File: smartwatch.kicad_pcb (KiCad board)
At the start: 2 copper layers, 40 x 40 mm, 46 parts, among them IC1 LTC4413EDD-1#PBF, IC2 MIA-M10Q-00B, J1 Conn_01x01_Pin, J2 Conn_01x01_Pin, J3 5022441530, J5 Conn_01x04_Socket, U1 NRF52832-QFAA-R, U10 AP2127K-1.8, U2 AP2112K-3.3TRG1, U3 MAX30102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

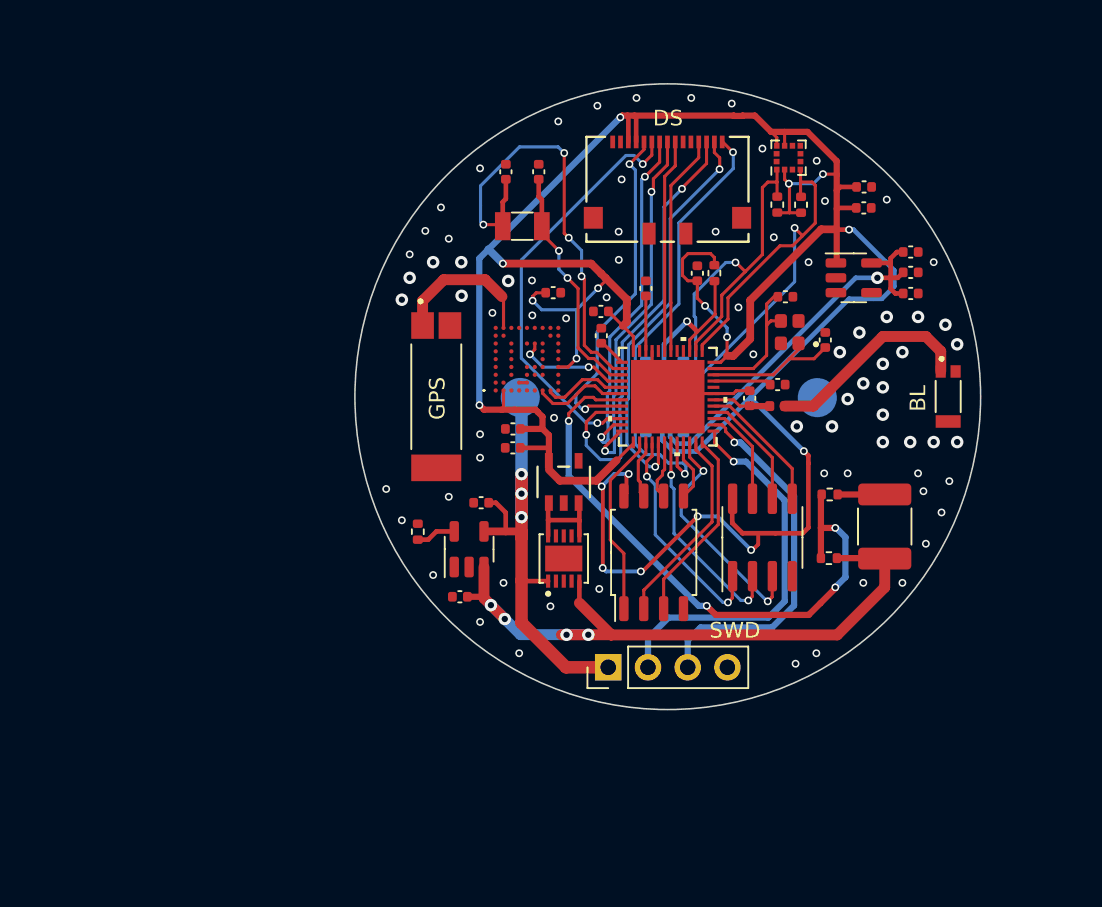
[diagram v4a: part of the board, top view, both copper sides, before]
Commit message: changed gps module
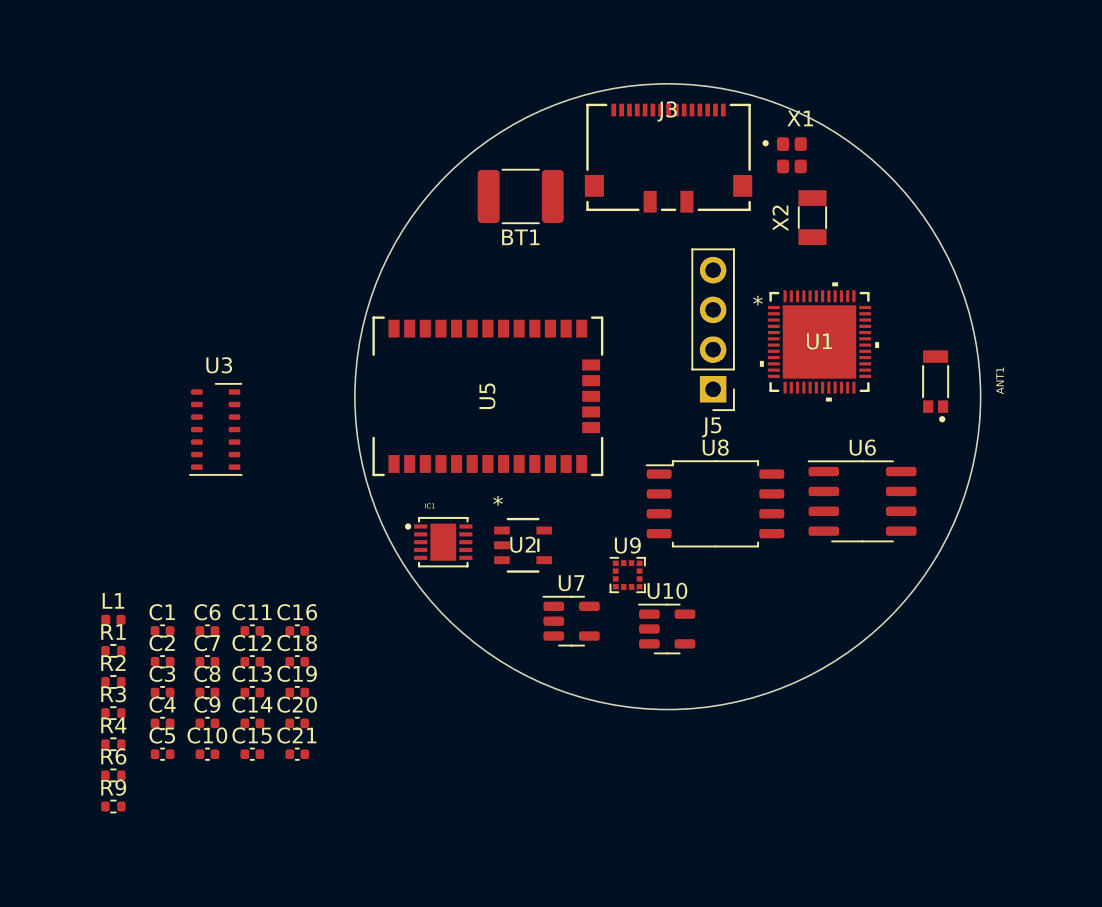
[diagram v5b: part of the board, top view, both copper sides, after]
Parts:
- removed C17: 1uF, Capacitor_SMD:C_0402_1005Metric
- removed E1: W3010, W3010:XCVR_W3010
- removed IC2: MIA-M10Q-00B, KiCad:MIAM10Q00B
- removed J1, J2: Conn_01x01_Pin, power_pad:power_pad_5mm
- added C10: 0.8pF, Capacitor_SMD:C_0402_1005Metric, F.Cu at (129.6, 115.5)
- added U5: CAM-M8C-0, CAM-M8C:QFN_M8C-0_UBL, F.Cu at (147.5, 92.6)
- U3: moved to F.Cu
- moved C5 56.8 mm to (126.7, 115.5)
- moved C4 56.5 mm to (126.7, 113.5)
- moved R3 54.7 mm to (123.6, 112.8), turned to 0 degrees
- moved C8 53.0 mm to (129.6, 111.5)
- moved R1 51.1 mm to (123.6, 108.8), turned to 0 degrees
- moved C7 50.7 mm to (129.6, 109.5)
- moved R9 49.9 mm to (123.6, 118.8), turned to 0 degrees
- moved C12 48.9 mm to (132.4, 109.5)
- moved R4 47.3 mm to (123.6, 114.8), turned to 0 degrees
- moved R2 46.5 mm to (123.6, 110.8), turned to 0 degrees
- moved C15 45.2 mm to (132.4, 115.5), turned to 0 degrees
- moved L1 44.6 mm to (123.6, 106.9)
- moved C14 43.6 mm to (132.4, 113.5)
- moved C3 41.1 mm to (126.7, 111.5), turned to 0 degrees
- moved C9 40.4 mm to (129.6, 113.5), turned to 0 degrees
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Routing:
- net +3.3V: track 197.0 -> 0.00 mm, vias 18 -> 0
- net Net-(BT1-+): track 43.1 -> 0.00 mm, vias 4 -> 0
- net /BT_V: track 38.7 -> 0.00 mm, vias 4 -> 0
- net /AC_SDA: track 30.7 -> 0.00 mm, vias 1 -> 0
- net /SWD_VCC: track 30.6 -> 0.00 mm, vias 3 -> 0
- net Net-(U1-P0.00): track 29.3 -> 0.00 mm, vias 4 -> 0
- net /TP_INT: track 29.1 -> 0.00 mm, vias 2 -> 0
- net Net-(U10-VOUT): track 28.9 -> 0.00 mm, vias 1 -> 0
- net /TP_SCL: track 28.7 -> 0.00 mm, vias 2 -> 0
- net /DISPLAY_CS: track 26.9 -> 0.00 mm, vias 2 -> 0
- net /TP_SDA: track 25.9 -> 0.00 mm, vias 2 -> 0
- net /AC_SCL: track 24.9 -> 0.00 mm, vias 1 -> 0
- net Net-(J5-Pin_2): track 24.8 -> 0.00 mm, vias 1 -> 0
- net /DISPLAY_SDI: track 23.6 -> 0.00 mm, vias 2 -> 0
- net Net-(J5-Pin_3): track 23.6 -> 0.00 mm, vias 1 -> 0
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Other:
- board text removed: "BL"
- board text removed: "DS"
- board text removed: "Designed By - Iiro Karppanen -"
- board text removed: "GPS"
- board text removed: "SWD"

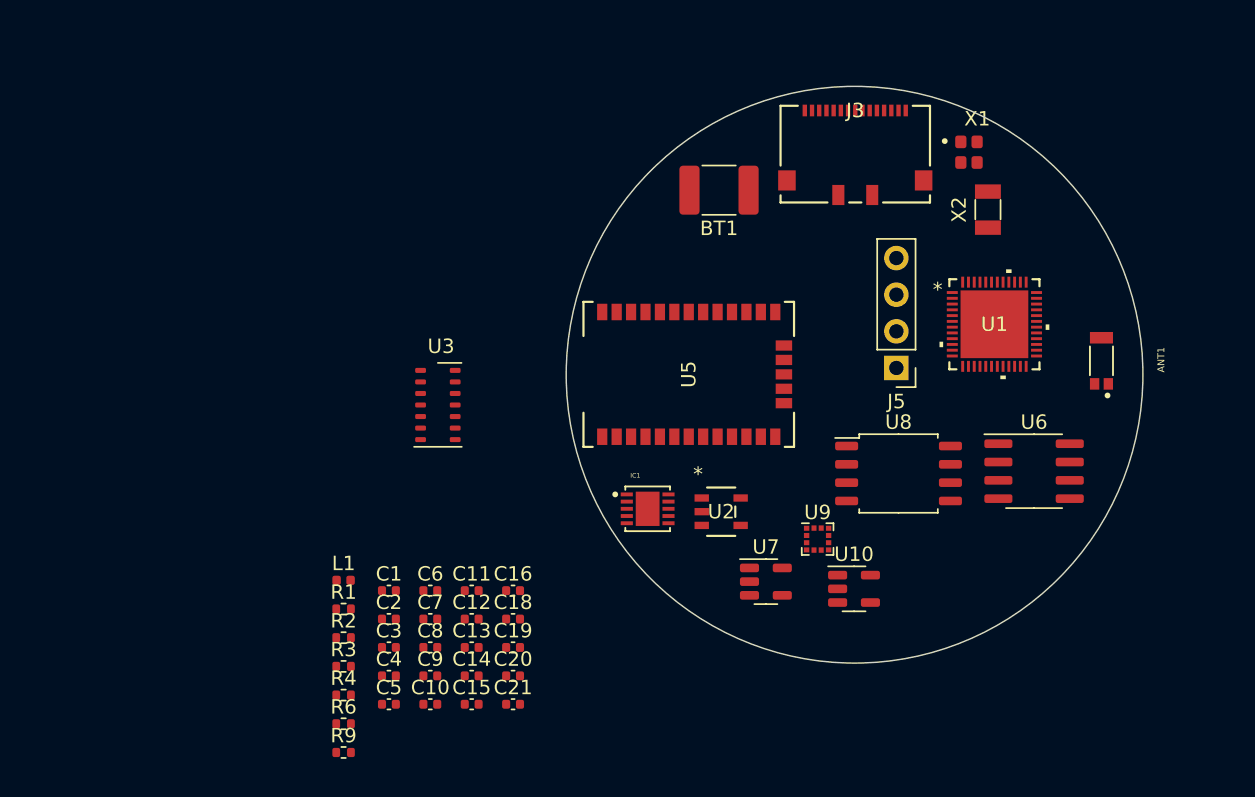
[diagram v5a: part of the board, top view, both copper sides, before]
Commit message: New rtc module
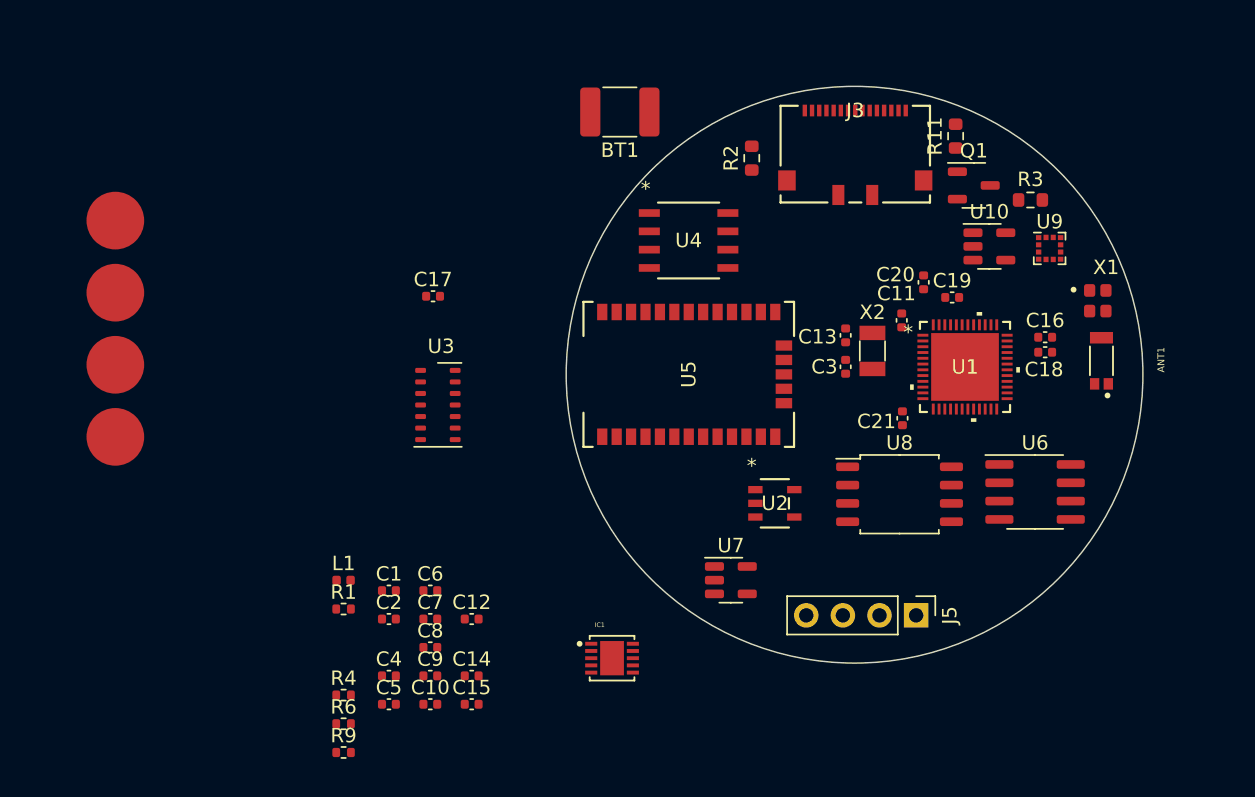
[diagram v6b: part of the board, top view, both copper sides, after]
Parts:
- added C17: 4.7uF, Capacitor_SMD:C_0402_1005Metric, F.Cu at (129.8, 87.2)
- added J1: Conn_01x01_Pin, power_pad:power_pad_4mm, F.Cu at (107.7, 81.9)
- added J2: Conn_01x01_Pin, power_pad:power_pad_4mm, F.Cu at (107.7, 86.9)
- added J4: Conn_01x01_Pin, power_pad:power_pad_4mm, F.Cu at (107.7, 91.9)
- added J6: Conn_01x01_Pin, power_pad:power_pad_4mm, F.Cu at (107.7, 96.9)
- added Q1: 2N7002-7-F, Package_TO_SOT_SMD:SOT-23-3, F.Cu at (167.3, 79.5)
- added R11: 10k, Resistor_SMD:R_0603_1608Metric, F.Cu at (166.0, 76.0)
- added U4: DS1302Z+T&R, DS1302Z+T&R:21-0041B_8_MXM, F.Cu at (147.5, 83.3)
- R2: value 3.3k -> 22; footprint Resistor_SMD:R_0402_1005Metric -> Resistor_SMD:R_0603_1608Metric
- R3: value 3.3k -> 10k; footprint Resistor_SMD:R_0402_1005Metric -> Resistor_SMD:R_0603_1608Metric
- moved R3 57.6 mm to (171.2, 80.5)
- moved R2 43.7 mm to (151.9, 77.6), turned to 90 degrees
- moved C18 41.3 mm to (172.2, 91.0)
- moved C16 40.9 mm to (172.2, 90.0)
- moved C20 39.4 mm to (163.8, 86.2), turned to 90 degrees
- moved C19 38.9 mm to (165.8, 87.2)
- moved C3 37.2 mm to (158.4, 92.0), turned to 90 degrees
- moved C11 35.2 mm to (162.3, 88.8), turned to 90 degrees
- moved C13 33.8 mm to (158.4, 89.9), turned to 90 degrees
- moved C21 33.5 mm to (162.3, 95.6), turned to 90 degrees
- moved U9 25.8 mm to (172.5, 83.8)
- moved U10 25.5 mm to (168.3, 83.7)
- moved J5 17.2 mm to (163.3, 109.3), turned to -90 degrees
- moved X1 13.6 mm to (175.9, 87.5)
- moved X2 12.7 mm to (160.2, 91.0), turned to -90 degrees
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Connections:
- net /SWD_VCC renamed VBUS
- J3 pad 2: GND -> /LEDK
- J3 pad 3: +3.3V -> Net-(J3-Pad3)
- J3 pad 4: +3.3V -> unconnected-(J3-Pad4)
- R1 pad 1: /AC_SCL -> unconnected-(R1-Pad1)
- R1 pad 2: +3.3V -> unconnected-(R1-Pad2)
- R2 pad 1: /HR_INT -> +3.3V
- R2 pad 2: +3.3V -> Net-(J3-Pad3)
- R3 pad 1: /AC_SDA -> Net-(Q1-G)
- R3 pad 2: +3.3V -> /BACKLIGHT_EN
- U1 pad 4: /GPS_IO -> unconnected-(U1-P0.02-Pad4)
- U1 pad 5: /GPS_RX -> unconnected-(U1-P0.03-Pad5)
- U1 pad 6: /GPS_TX -> unconnected-(U1-P0.04-Pad6)
- U5 pad 1: unconnected-(U5-Pad1) -> +3.3V
- U5 pad 10: unconnected-(U5-Pad10) -> GND
- U5 pad 11: unconnected-(U5-Pad11) -> GND
- U5 pad 12: unconnected-(U5-Pad12) -> GND
- U5 pad 13: unconnected-(U5-Pad13) -> GND
- U5 pad 14: unconnected-(U5-Pad14) -> GND
- U5 pad 15: unconnected-(U5-Pad15) -> GND
- U5 pad 16: unconnected-(U5-Pad16) -> Net-(U5-Pad16)
- U5 pad 17: unconnected-(U5-Pad17) -> Net-(U5-Pad16)
- U5 pad 18: unconnected-(U5-Pad18) -> GND
- U5 pad 19: unconnected-(U5-Pad19) -> GND
- U5 pad 21: unconnected-(U5-Pad21) -> GND
- U5 pad 22: unconnected-(U5-Pad22) -> GND
- U5 pad 23: unconnected-(U5-Pad23) -> Net-(R8-Pad1)
- U5 pad 25: unconnected-(U5-Pad25) -> Net-(R7-Pad1)
- U5 pad 26: unconnected-(U5-Pad26) -> Net-(R5-Pad1)
- U5 pad 27: unconnected-(U5-Pad27) -> GND
- U5 pad 31: unconnected-(U5-Pad31) -> GND
- U5 pad 4: unconnected-(U5-Pad4) -> GND
- U5 pad 5: unconnected-(U5-Pad5) -> GND
- U5 pad 7: unconnected-(U5-Pad7) -> Net-(R10-Pad2)
- U5 pad 8: unconnected-(U5-Pad8) -> +3.3V
- U5 pad 9: unconnected-(U5-Pad9) -> +3.3V

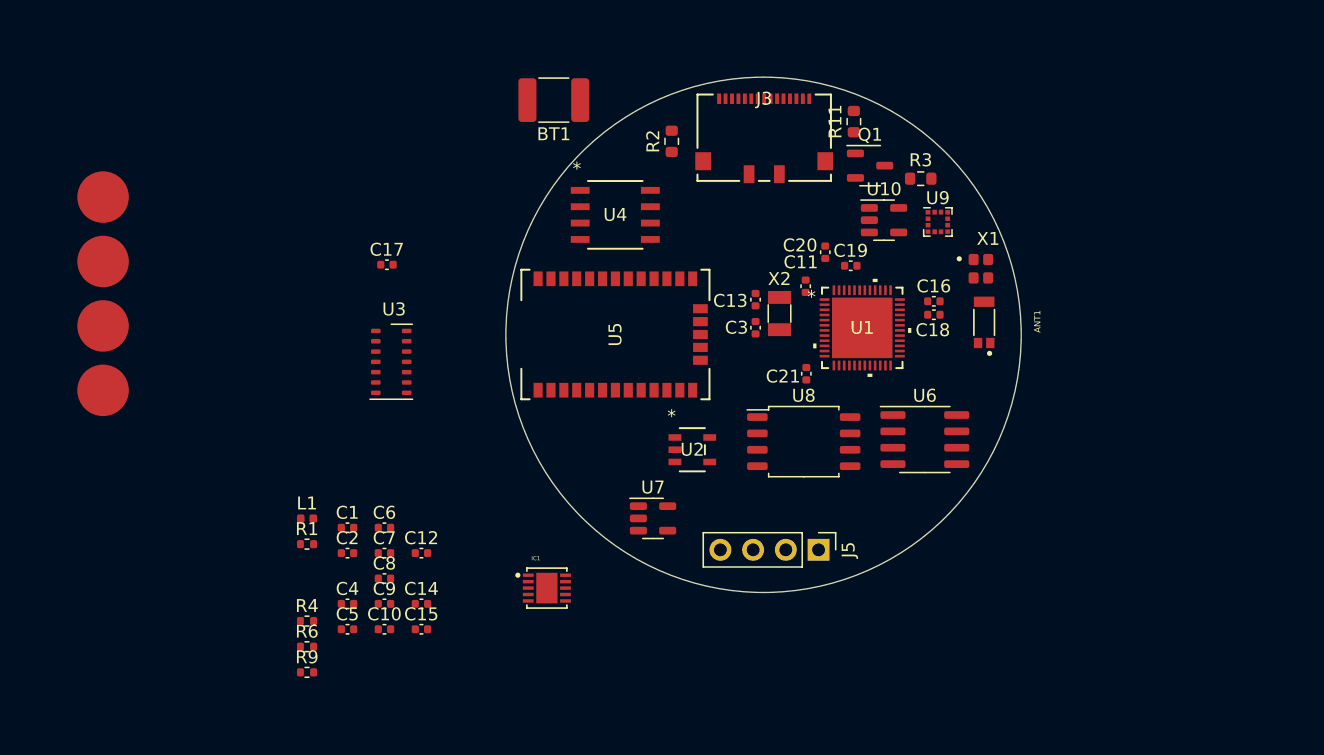
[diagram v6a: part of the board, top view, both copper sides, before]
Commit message: changed to nrf5340 & did some rework to charging circuit
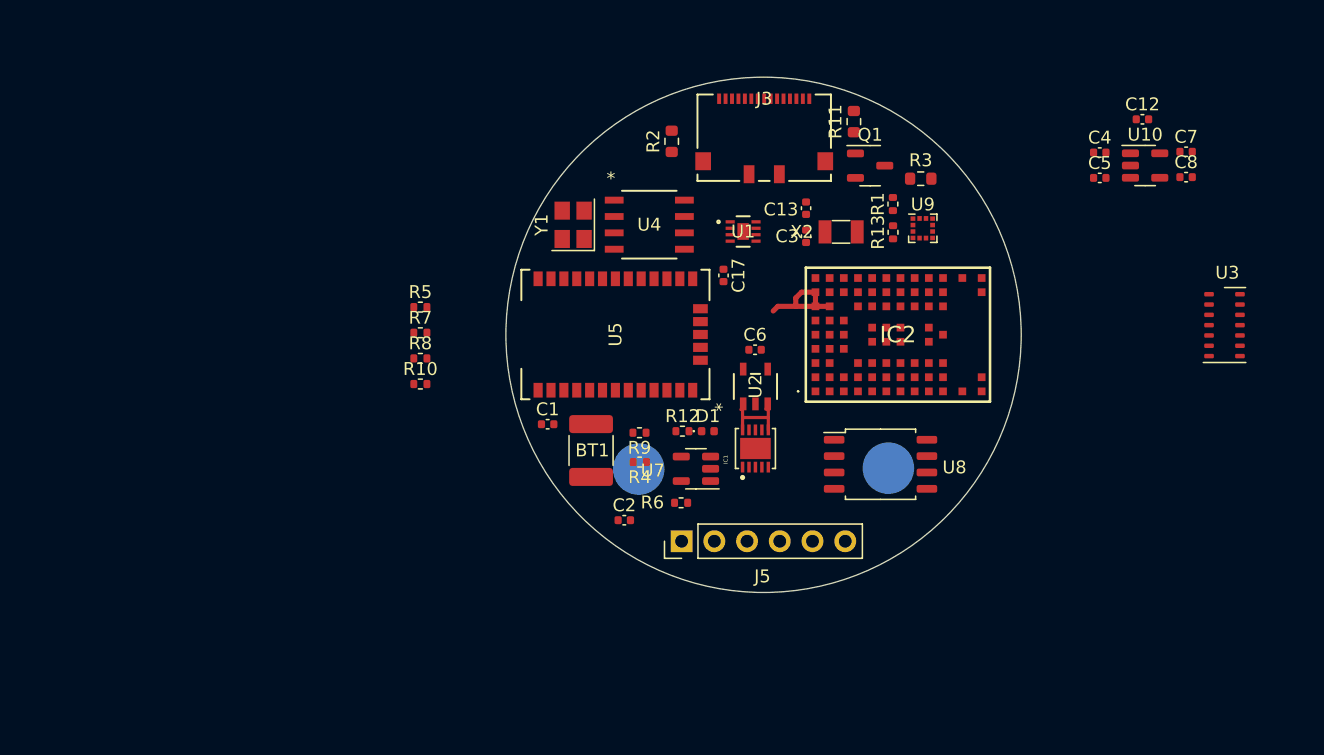
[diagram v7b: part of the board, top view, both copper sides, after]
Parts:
- removed ANT1: W3008, W3008:ANTENNA_W3008
- removed C10, C9: 0.8pF, Capacitor_SMD:C_0402_1005Metric
- removed C11, C16, C21: 100nF, Capacitor_SMD:C_0402_1005Metric
- removed C14, C15: 12pF, Capacitor_SMD:C_0402_1005Metric
- removed C18: 100pF, Capacitor_SMD:C_0402_1005Metric
- removed C19: 1uF, Capacitor_SMD:C_0402_1005Metric
- removed C20: 4.7uF, Capacitor_SMD:C_0402_1005Metric
- removed J4, J6: Conn_01x01_Pin, power_pad:power_pad_4mm
- removed L1: 3.9nH, Inductor_SMD:L_0402_1005Metric
- removed U6: ESP-PSRAM64, Package_SO:SOIC-8_3.9x4.9mm_P1.27mm
- removed X1: CX2016DB32000D0WZRC1, CX2016DB32000D0WZRC1:OSCCC200X160X45N
- added D1: LED_GREEN, LED_SMD:LED_0402_1005Metric, F.Cu at (154.7, 100.1)
- added IC2: NORA-B120-00B, NORA-B120-00B:NORAB12000B, F.Cu at (169.4, 92.6)
- added R10: 220, Resistor_SMD:R_0402_1005Metric, F.Cu at (132.4, 96.4)
- added R12: 470, Resistor_SMD:R_0402_1005Metric, F.Cu at (152.7, 100.1)
- added R13: 3.3k, Resistor_SMD:R_0402_1005Metric, F.Cu at (169.1, 84.6)
- added R5: 220, Resistor_SMD:R_0402_1005Metric, F.Cu at (132.4, 90.5)
- added R7: 220, Resistor_SMD:R_0402_1005Metric, F.Cu at (132.4, 92.4)
- added R8: 220, Resistor_SMD:R_0402_1005Metric, F.Cu at (132.4, 94.4)
- added Y1: 32.768kHz, Crystal:Crystal_SMD_TXC_7M-4Pin_3.2x2.5mm, F.Cu at (144.2, 84.1)
- J1, J2: moved to B.Cu
- J5: value Conn_01x04_Socket -> Conn_01x06_Pin; footprint Connector_PinHeader_2.54mm:PinHeader_1x04_P2.54mm_Vertical -> Connector_PinHeader_2.54mm:PinHeader_1x06_P2.54mm_Vertical
- R6: value 5k -> 10k
- U1: value NRF52832-QFAA-R -> MAX17048G+T10; footprint NRF52832-QFAA-R:QFN-48_NOR -> MAX17048G_T10:21-0168E_T822-3_MXM
- moved C7 69.6 mm to (191.8, 78.4)
- moved C8 69.6 mm to (191.8, 80.4)
- moved C4 68.1 mm to (185.1, 78.5)
- moved C5 68.1 mm to (185.1, 80.4)
- moved C12 65.3 mm to (188.4, 75.9)
- moved U3 64.7 mm to (194.8, 91.8)
- moved J1 64.5 mm to (168.7, 102.9), turned to 180 degrees
- moved R1 52.6 mm to (169.0, 82.5), turned to 90 degrees
- moved J2 44.6 mm to (149.3, 103.0), turned to 180 degrees
- moved C6 31.9 mm to (158.3, 93.8)
- moved R9 31.8 mm to (149.4, 100.2), turned to 180 degrees
- moved R6 31.1 mm to (152.6, 105.6)
- moved R4 28.6 mm to (149.4, 102.5), turned to 180 degrees
- moved BT1 27.4 mm to (145.6, 101.6), turned to -90 degrees
- moved C17 26.1 mm to (155.9, 88.0), turned to -90 degrees
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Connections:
- net /RTX_CE renamed /RTC_CE
- net /RTX_IO renamed /RTC_IO
- net /RTX_SCLK renamed /RTC_SCLK
- C13 pad 2: Net-(U1-P0.00) -> Net-(IC2-P0.01/XL2)
- C17 pad 1: +3.3V -> VSYS
- C2 pad 1: VBUS -> Net-(IC1-INA)
- C3 pad 2: Net-(U1-P0.01) -> Net-(IC2-P0.00/XL1)
- C4 pad 1: +3.3V -> VSYS
- C5 pad 1: +3.3V -> VSYS
- C6 pad 1: +3.3V -> VSYS
- IC1 pad 1: VBUS -> Net-(IC1-INA)
- J2 pad 1: VBUS -> Net-(IC1-INA)
- J5 pad 2: Net-(J5-Pin_2) -> /SWDIO
- J5 pad 3: Net-(J5-Pin_3) -> /SWDCLK
- J5 pad 4: GND -> /SWO
- R1 pad 1: unconnected-(R1-Pad1) -> /AC_SDA
- R1 pad 2: unconnected-(R1-Pad2) -> +3.3V
- R2 pad 1: +3.3V -> VSYS
- U1 pad 1: Net-(U1-DEC1) -> unconnected-(U1-CTG-Pad1)
- U1 pad 2: Net-(U1-P0.00) -> unconnected-(U1-CELL-Pad2)
- U1 pad 3: Net-(U1-P0.01) -> unconnected-(U1-VDD-Pad3)
- U1 pad 7: /BT_V -> unconnected-(U1-SCL-Pad7)
- U1 pad 8: /DISPLAY_D/C -> unconnected-(U1-SDA-Pad8)
- U1 pad 9: /TP_INT -> unconnected-(U1-EPAD-Pad9)
- U10 pad 1: +3.3V -> VSYS
- U2 pad 5: +3.3V -> VSYS
- U3 pad 10: +3.3V -> VSYS
- U3 pad 9: +3.3V -> VSYS
- U5 pad 1: +3.3V -> VSYS
- U5 pad 8: +3.3V -> VSYS
- U5 pad 9: +3.3V -> VSYS
- U7 pad 1: unconnected-(U7-STAT-Pad1) -> Net-(D1-K)
- U7 pad 4: VBUS -> Net-(IC1-INA)
- U9 pad 10: +3.3V -> VSYS
- U9 pad 2: +3.3V -> VSYS
- U9 pad 9: +3.3V -> VSYS
- X2 pad 1: Net-(U1-P0.01) -> Net-(IC2-P0.00/XL1)
- X2 pad 2: Net-(U1-P0.00) -> Net-(IC2-P0.01/XL2)
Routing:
- net VSYS: track 0.00 -> 8.00 mm
- net Net-(IC1-OUTA): track 0.00 -> 6.09 mm
